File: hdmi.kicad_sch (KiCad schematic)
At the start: 1 part

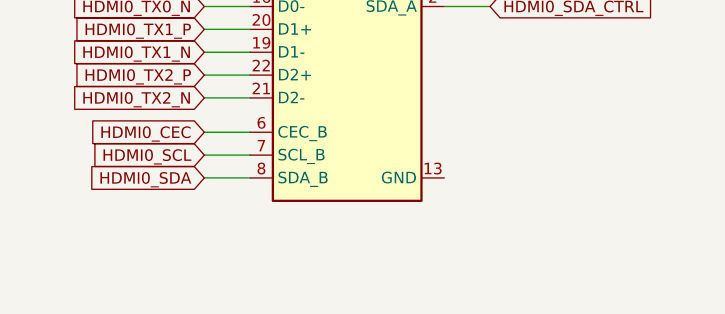
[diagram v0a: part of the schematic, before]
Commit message: [#53847] Connect PF SoC to CrossLink
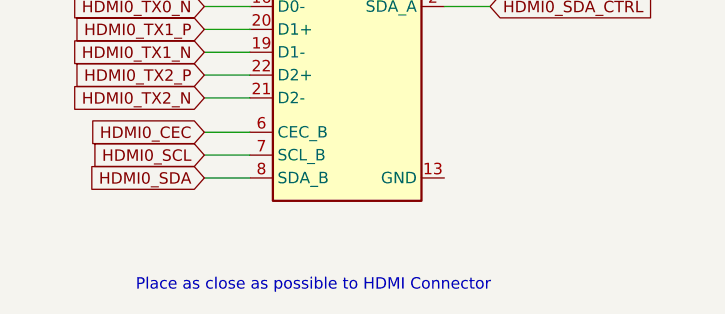
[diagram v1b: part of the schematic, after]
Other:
- note added: "Place as close as possible to HDMI Connector"
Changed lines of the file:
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@@
     (stroke (width 0) (type default) (color 0 0 0 0))
+  )
+  (text "Place as close as possible to HDMI Connector " (at 135.89 132.08 0)
+    (effects (font (size 1.27 1.27)) (justify left bottom))
   )
   (global_label "HDMI0_CEC_CTRL" (shape input) (at 175.26 95.25 0) (fields_autoplaced)

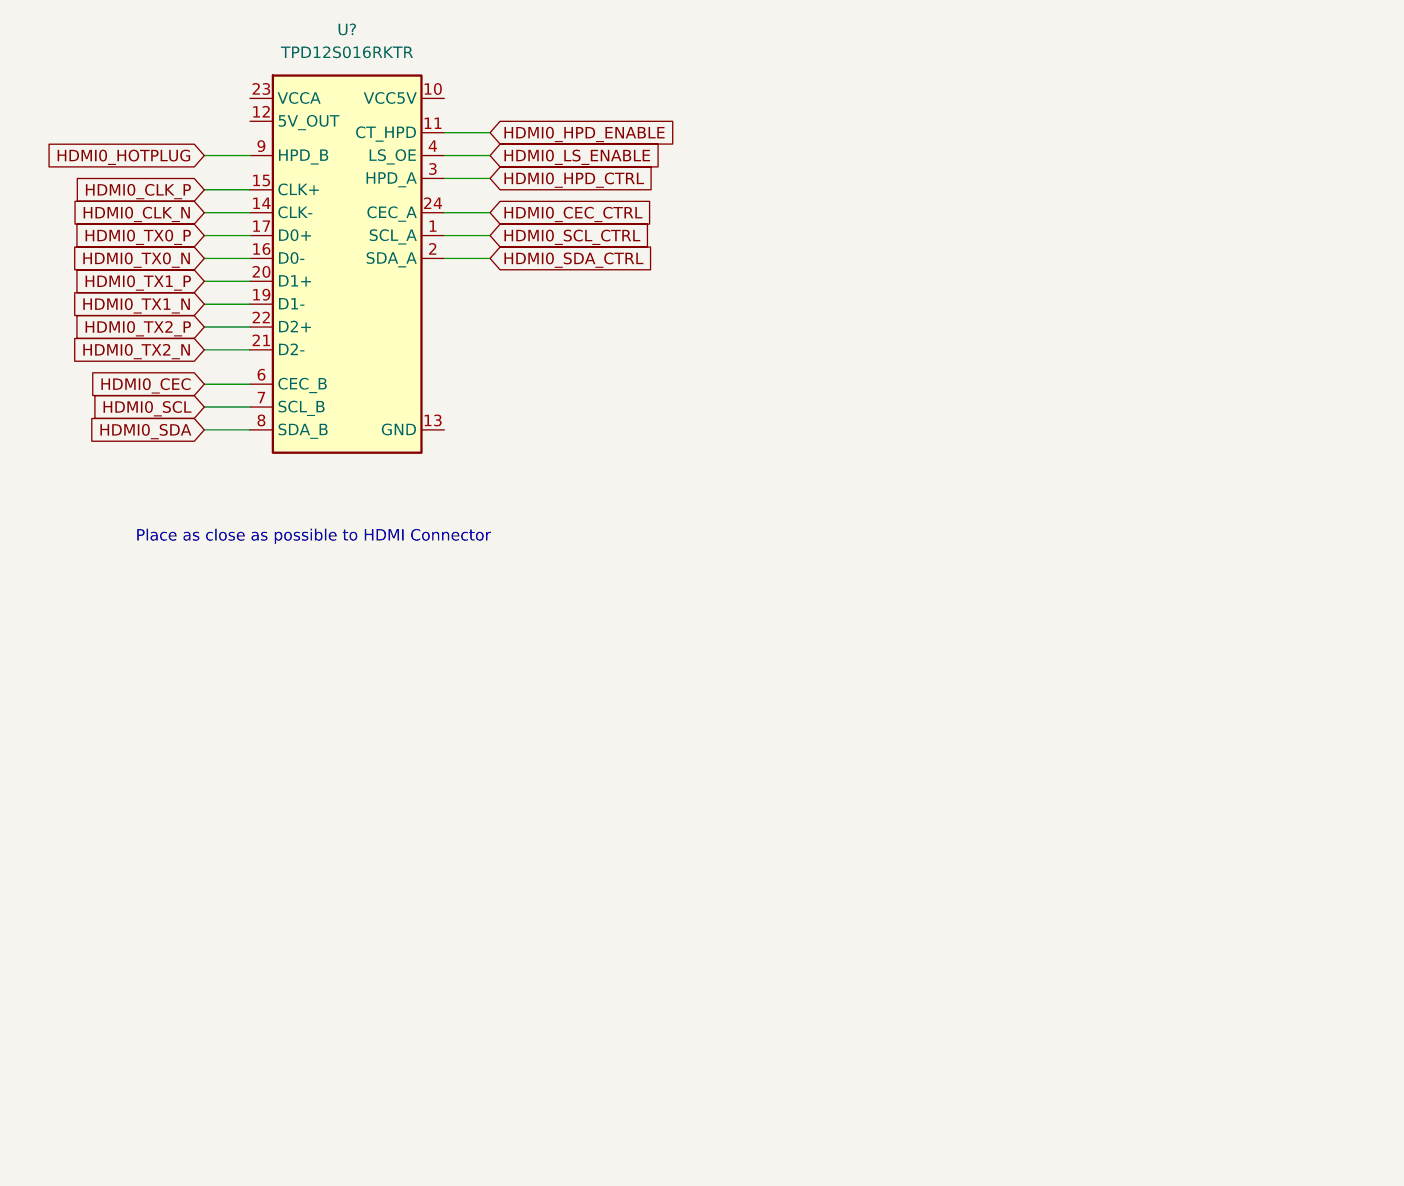
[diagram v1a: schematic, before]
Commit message: [#54084] Sheets cleanup
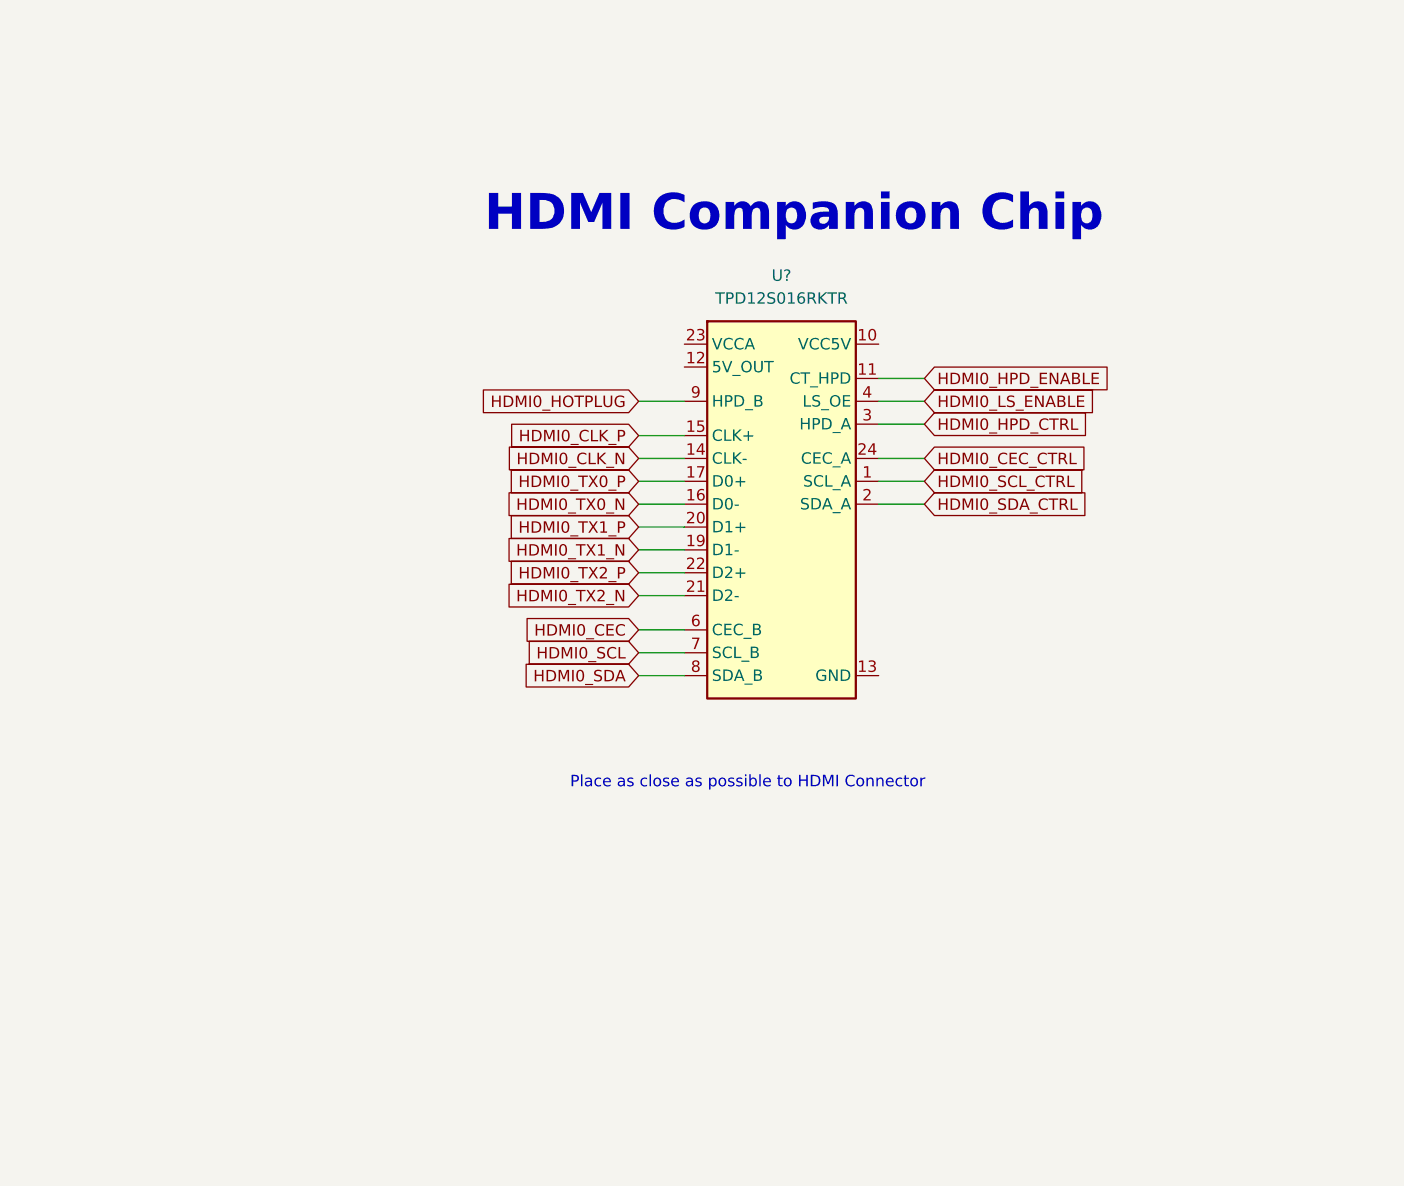
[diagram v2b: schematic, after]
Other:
- note added: "HDMI Companion Chip"
- company: (none) -> Antmicro Ltd
- title: (none) -> PolarFire SoM
- moved on the sheet: U?

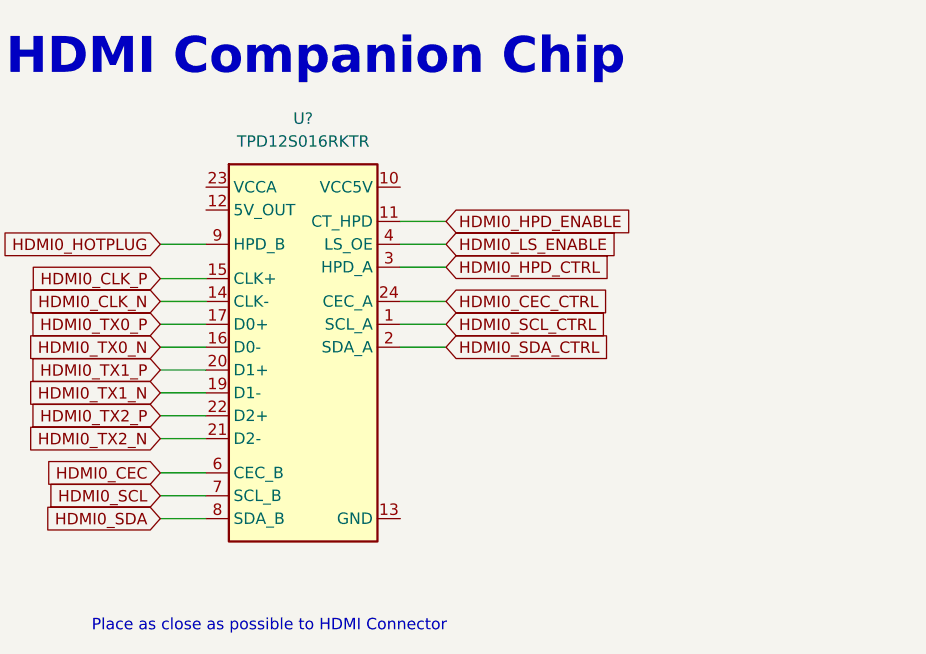
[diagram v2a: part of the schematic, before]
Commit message: [#54016] Connect power to HDMI Companion Chip
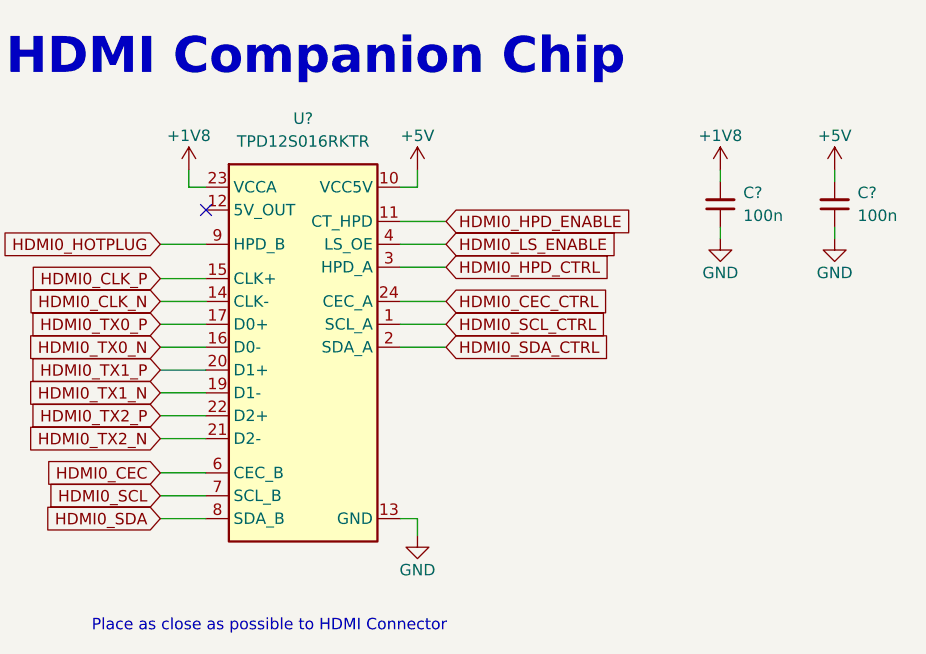
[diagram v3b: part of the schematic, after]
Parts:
- added C? (x2): C_100n_0402, antmicro-footprints:C_0402_1005Metric, symbol antmicroCapacitors0402:C_100n_0402
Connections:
- net +5V: now reaches U?.10 (VCC5V)
- net +5V: now also C?.2
- net GND: now reaches U?.13 (GND), U?.18 (GND), U?.5 (GND)
- net GND: now also C?.1, C?.1
- net +1V8: now reaches U?.23 (VCCA)
- net +1V8: now also C?.2
- no-connect marks 0 -> 1

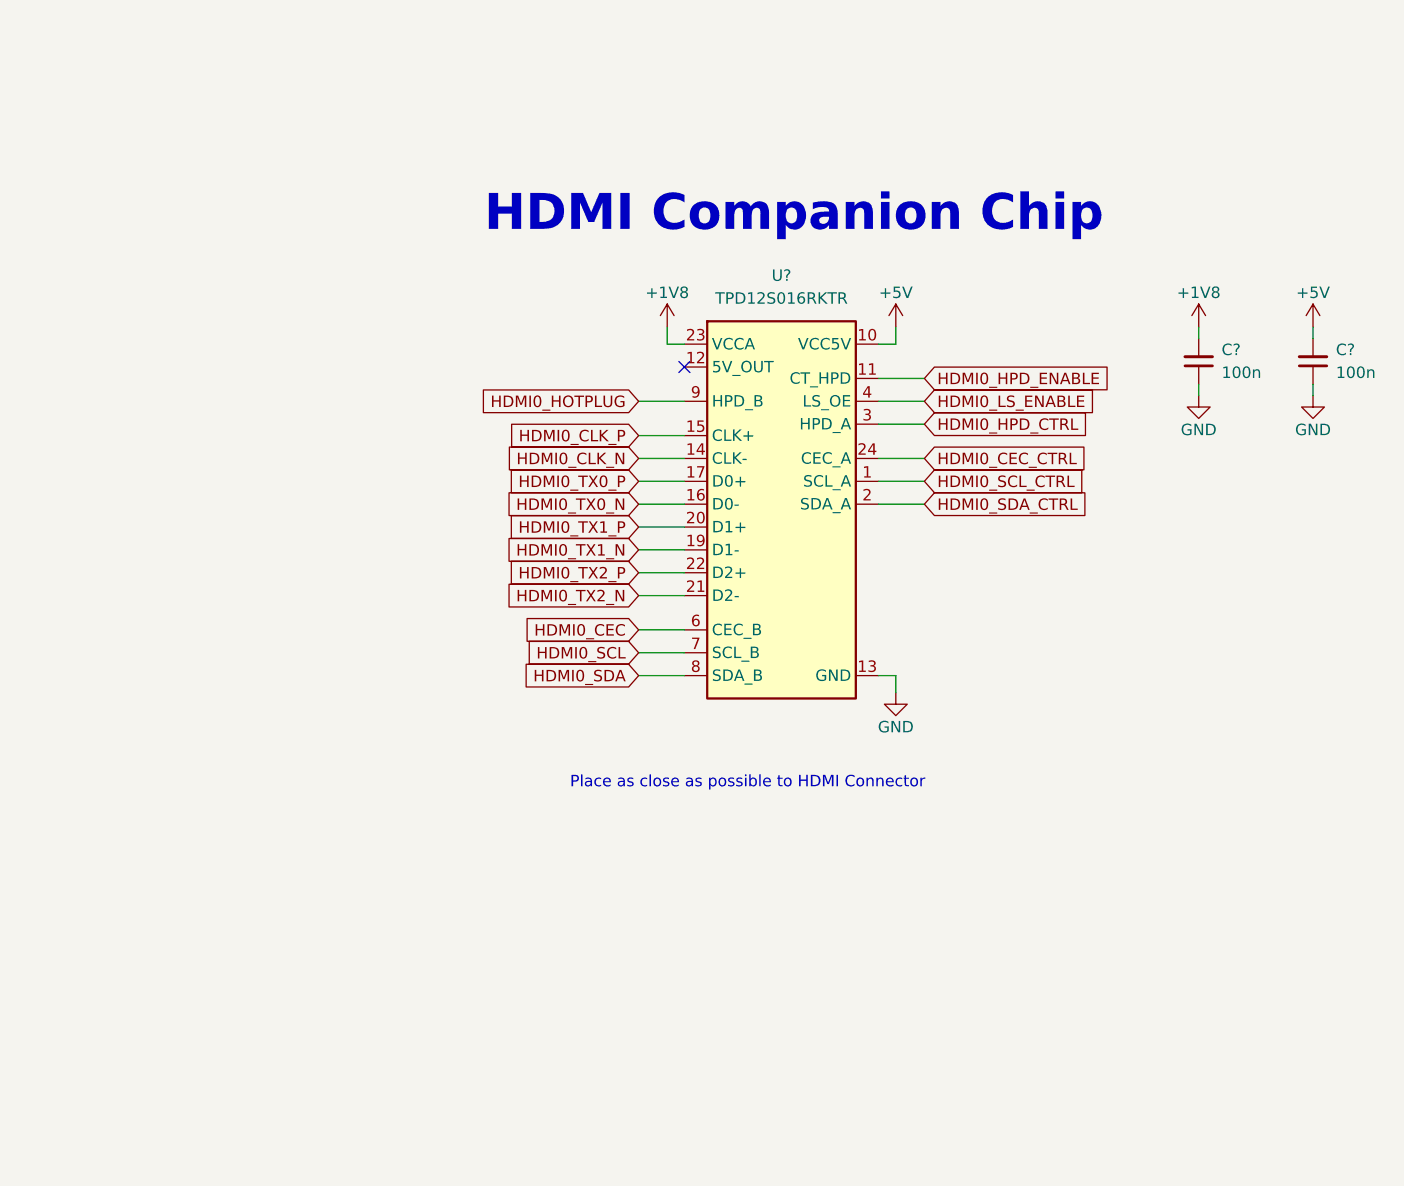
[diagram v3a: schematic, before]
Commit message: [#53847] Add HDMI TVS diodes
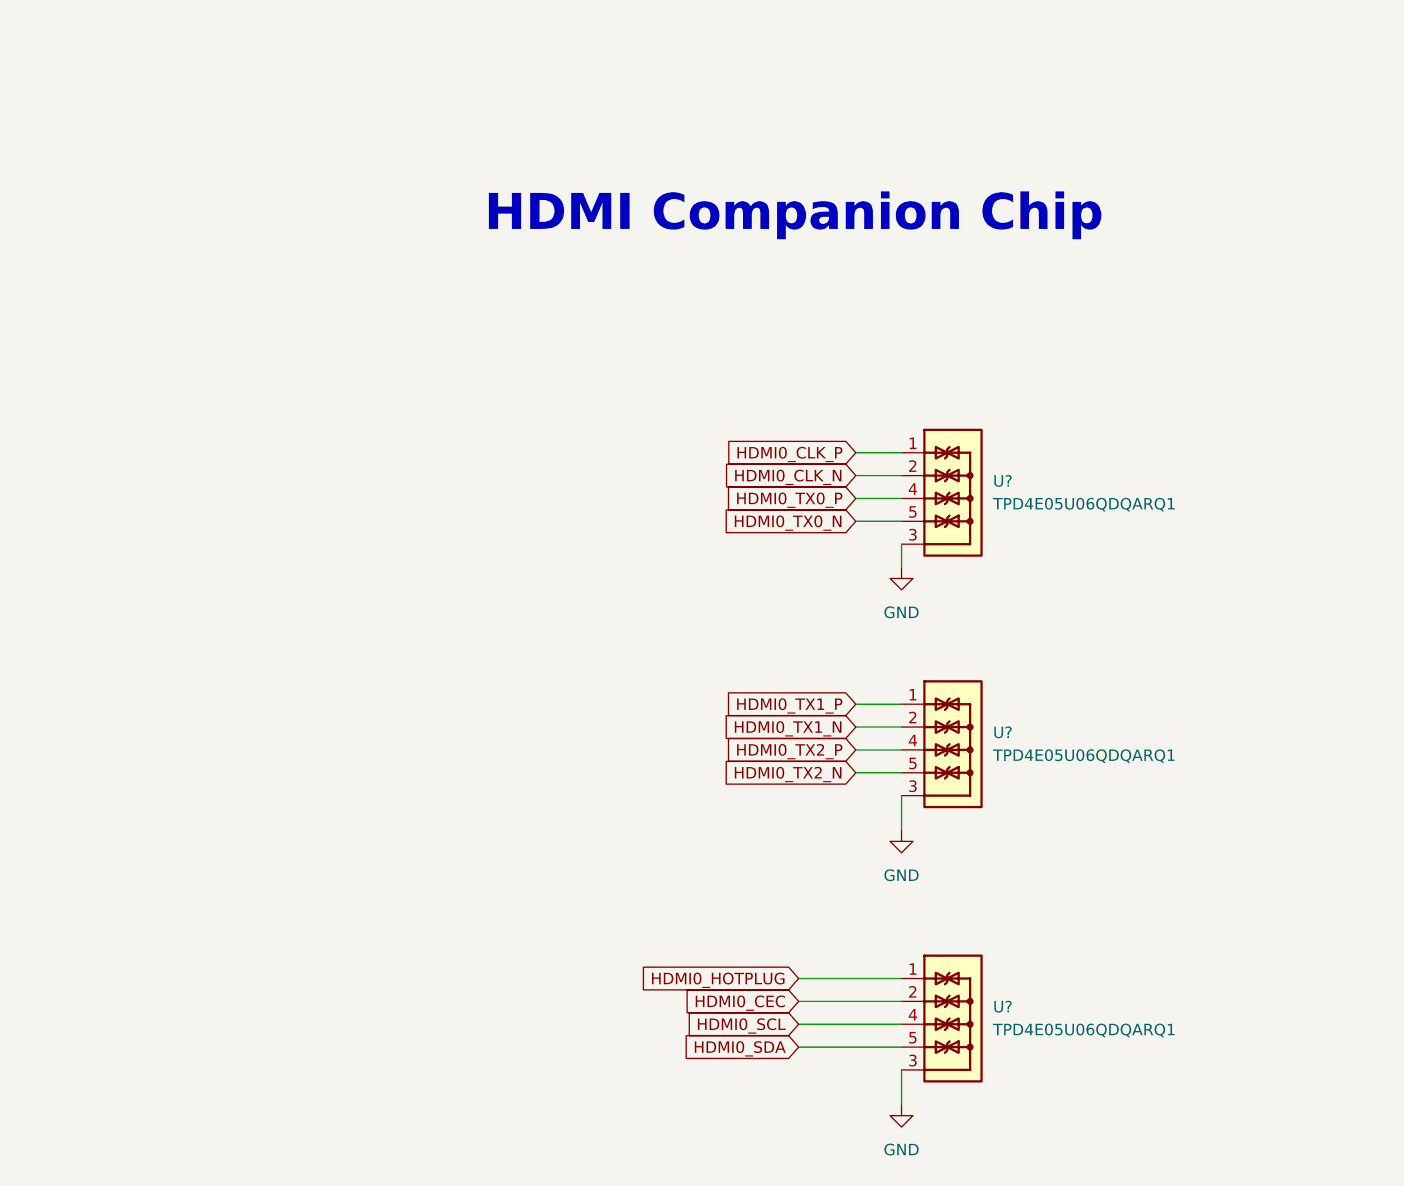
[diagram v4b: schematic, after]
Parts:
- removed C? (x2): C_100n_0402, antmicro-footprints:C_0402_1005Metric, symbol antmicroCapacitors0402:C_100n_0402
- removed U?: TPD12S016_QFN, antmicro-footprints:UQFN-24_2x4mm_Layout2x10, symbol antmicroLogicTranslatorsLevelShifters:TPD12S016_QFN
- added U? (x3): TPD4E05U06QDQARQ1, antmicro-footprints:USON-10_2.5x1mm_P0.5mm, symbol antmicroTVSDiodes:TPD4E05U06QDQARQ1
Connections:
- net GND: now also U?.3, U?.3, U?.3, U?.8, U?.8, U?.8
- net HDMI0_CEC: now also U?.2, U?.9
- net HDMI0_CLK_N: now also U?.2, U?.9
- net HDMI0_CLK_P: now also U?.1, U?.10
- net HDMI0_HOTPLUG: now also U?.1, U?.10
- net HDMI0_SCL: now also U?.4, U?.7
- net HDMI0_SDA: now also U?.5, U?.6
- net HDMI0_TX0_N: now also U?.5, U?.6
- net HDMI0_TX0_P: now also U?.4, U?.7
- net HDMI0_TX1_N: now also U?.2, U?.9
- net HDMI0_TX1_P: now also U?.1, U?.10
- net HDMI0_TX2_N: now also U?.5, U?.6
- net HDMI0_TX2_P: now also U?.4, U?.7
- no-connect marks 1 -> 0
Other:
- note removed: "Place as close as possible to HDMI Connector"
